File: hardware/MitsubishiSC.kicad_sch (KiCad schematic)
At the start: 68 parts, among them J1 CN105, J2 USB_C_Receptacle_USB2.0_16P, Q1 BSS138, Q2 BSS138, SW3 SPST, SW4 SPST, U1 TPS562203, U3 ESP32-C3-WROOM-02, U4 USBLC6-2SC6, U5 TLV75733PDBV

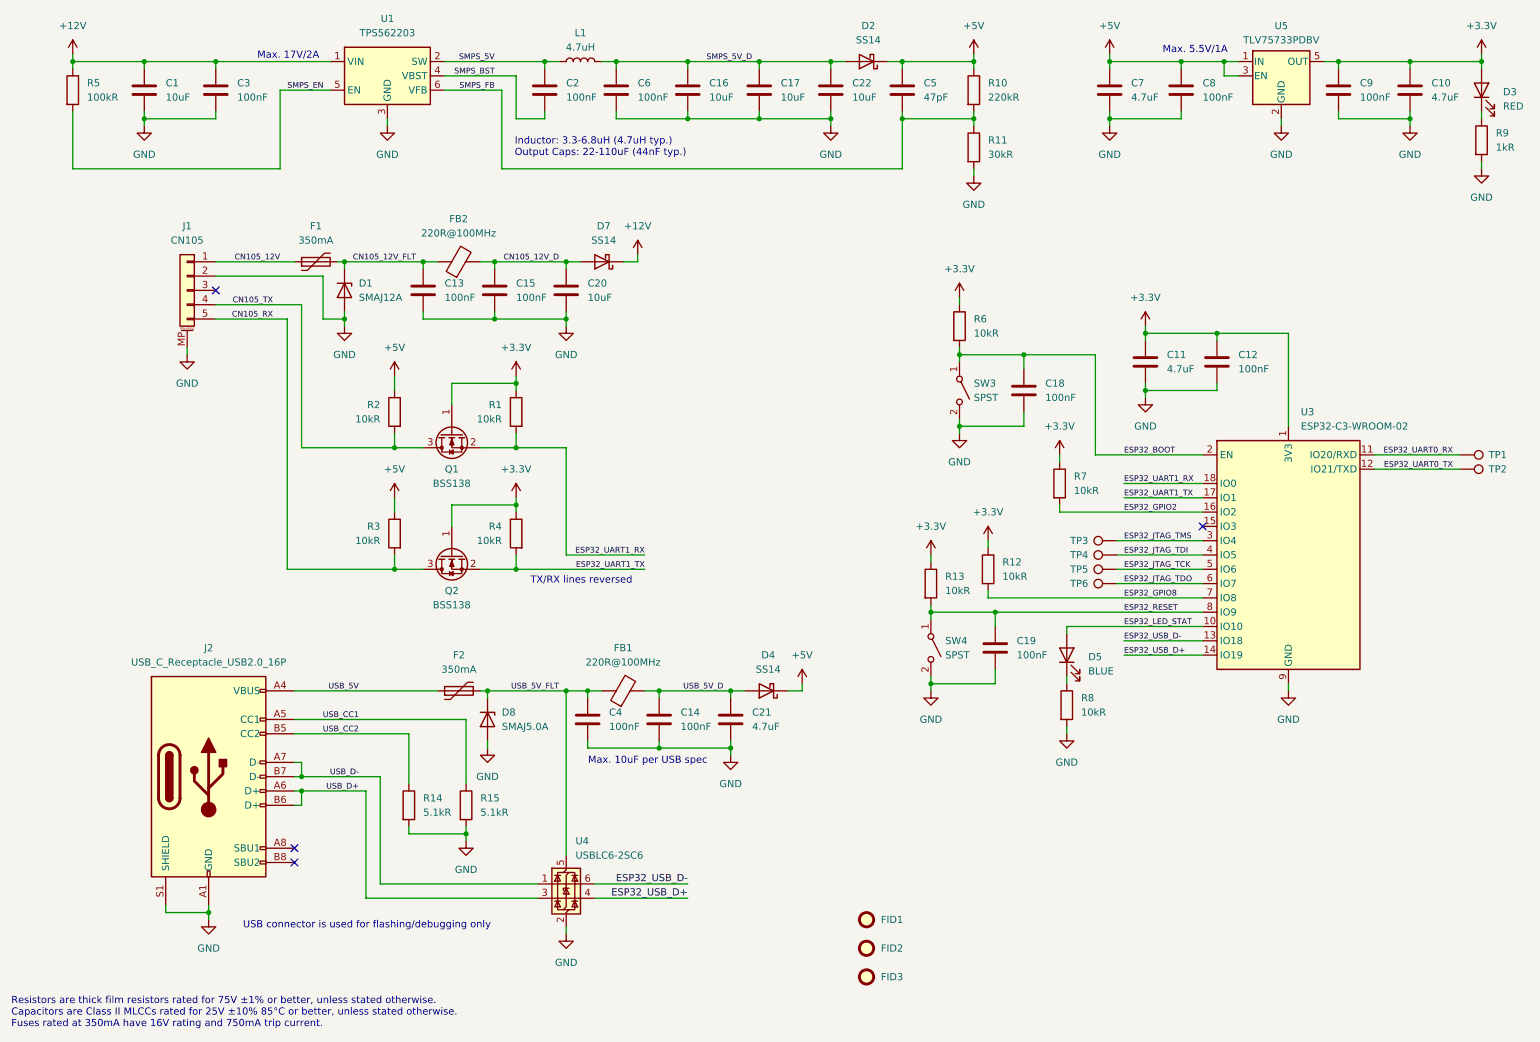
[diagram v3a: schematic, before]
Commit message: feat(pcb): revamp design and layout
This commit makes significant changes to the PCB, primarily changing the
MCU from ESP32-C3 to ESP32-C6 to accommodate Matter-over-Thread.
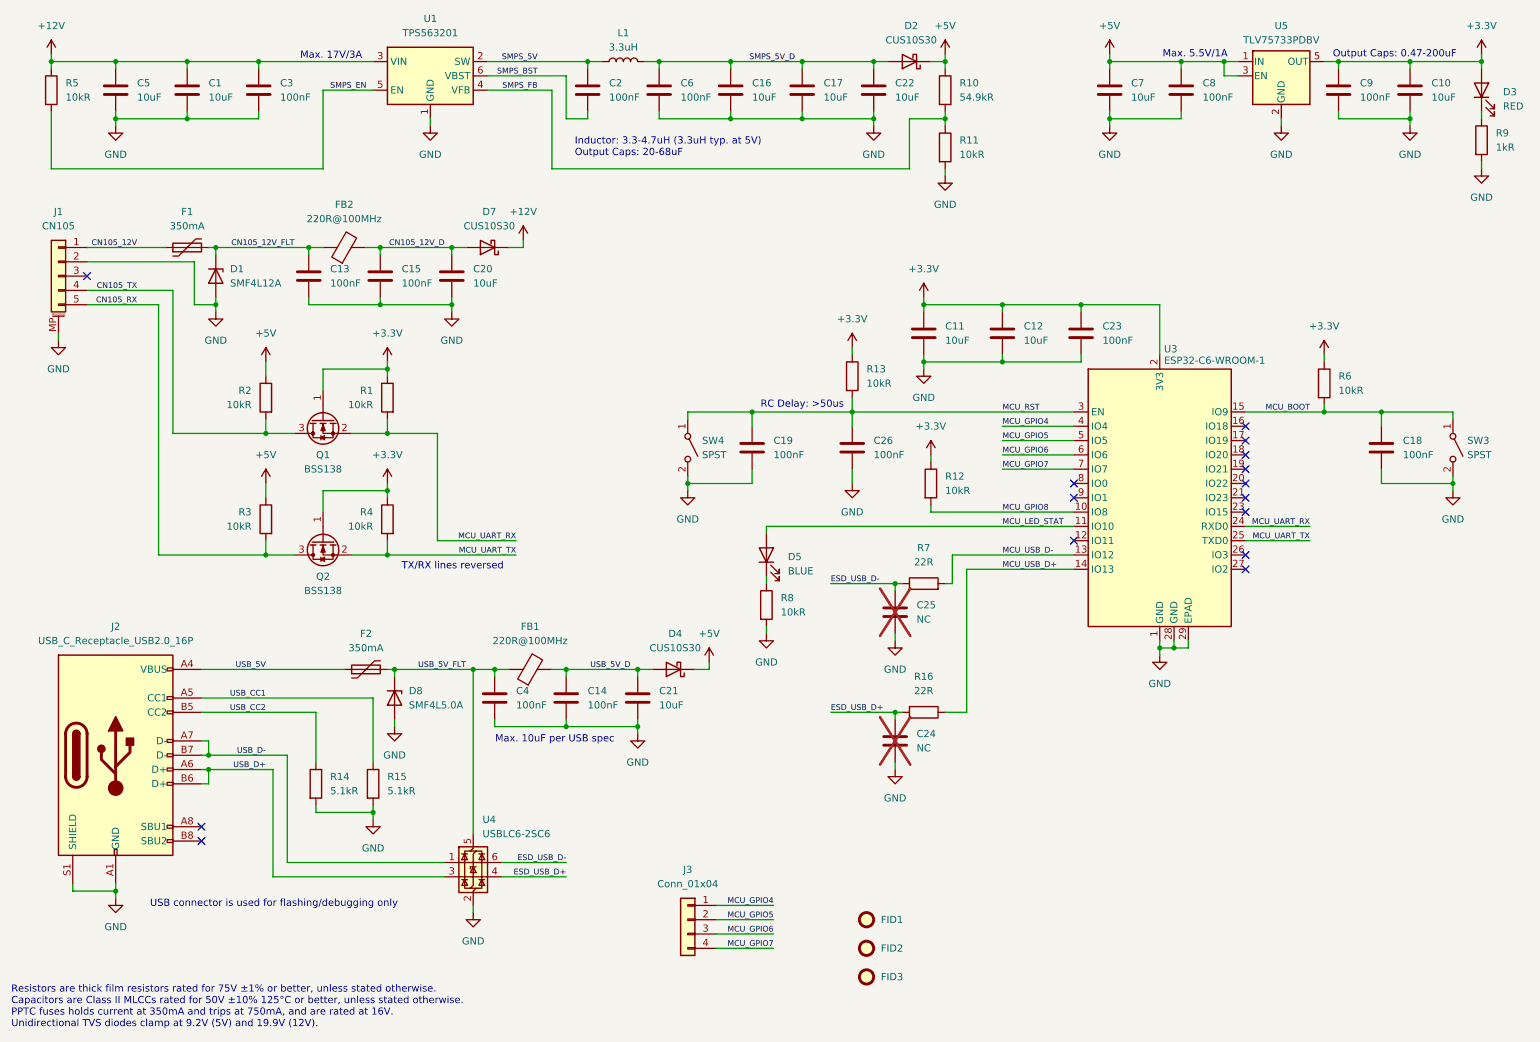
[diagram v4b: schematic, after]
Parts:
- removed TP1, TP2, TP3, TP4, TP5, TP6: TestPoint, TestPoint:TestPoint_Pad_D1.0mm, symbol Connector:TestPoint
- added C23, C26: 100nF, Capacitor_SMD:C_0603_1608Metric, symbol Device:C
- added C24, C25: NC, Capacitor_SMD:C_0603_1608Metric, symbol Device:C
- added J3: Conn_01x04, Connector_PinHeader_2.54mm:PinHeader_1x04_P2.54mm_Vertical, symbol Connector_Generic:Conn_01x04
- added R16: 22R, Resistor_SMD:R_0603_1608Metric, symbol Device:R
- C1, C16, C17, C20, C22: footprint Capacitor_SMD:C_0603_1608Metric -> Capacitor_SMD:C_1206_3216Metric; Distributor Part Number C344022 -> C89632; Manufacturer Murata Electronics -> Samsung Electro-Mechanics; Manufacturer Part Number GRM188R61E106KA73D -> CL31B106KBHNNNE
- C10, C11, C21, C7: value 4.7uF -> 10uF; footprint Capacitor_SMD:C_0603_1608Metric -> Capacitor_SMD:C_1206_3216Metric; Distributor Part Number C90057 -> C89632; Manufacturer Murata Electronics -> Samsung Electro-Mechanics; Manufacturer Part Number GRM188R61E475KE11D -> CL31B106KBHNNNE
- C12: value 100nF -> 10uF; footprint Capacitor_SMD:C_0603_1608Metric -> Capacitor_SMD:C_1206_3216Metric; Distributor Part Number C91183 -> C89632; Manufacturer YAGEO -> Samsung Electro-Mechanics; Manufacturer Part Number CC0603JRX7R9BB104 -> CL31B106KBHNNNE
- C13, C14, C15, C18, C19, C2, C3, C4, C6, C8, C9: Distributor Part Number C91183 -> C15725; Manufacturer YAGEO -> Samsung Electro-Mechanics; Manufacturer Part Number CC0603JRX7R9BB104 -> CL10B104KC8NNNC
- C5: value 47pF -> 10uF; footprint Capacitor_SMD:C_0603_1608Metric -> Capacitor_SMD:C_1206_3216Metric; Distributor Part Number C1671 -> C89632; Manufacturer Part Number CL10C470JB8NNNC -> CL31B106KBHNNNE
- D1: value SMAJ12A -> SMF4L12A; footprint Diode_SMD:D_SMA -> Diode_SMD:D_SOD-123F; Distributor Part Number C148213 -> C1972952; Manufacturer Part Number SMAJ12A -> SMF4L12A
- D2, D4, D7: value SS14 -> CUS10S30; footprint Diode_SMD:D_SMA -> Diode_SMD:D_SOD-323; Distributor Part Number C83852 -> C146335; Manufacturer onsemi -> TOSHIBA; Manufacturer Part Number SS14 -> CUS10S30,H3F
- D8: value SMAJ5.0A -> SMF4L5.0A; footprint Diode_SMD:D_SMA -> Diode_SMD:D_SOD-123F; Distributor Part Number C83329 -> C1976930; Manufacturer Part Number SMAJ5.0A -> SMF4L5.0A
- L1: value 4.7uH -> 3.3uH
- R10: value 220kR -> 54.9kR; Distributor Part Number C107696 -> C185321; Manufacturer Part Number RC0603FR-07220RL -> RC0603FR-0754K9L
- R11: value 30kR -> 10kR; Distributor Part Number C128060 -> C98220; Manufacturer Part Number RC0603FR-0730RL -> RC0603FR-0710KL
- R5: value 100kR -> 10kR; Distributor Part Number C14675 -> C98220; Manufacturer Part Number RC0603FR-07100KL -> RC0603FR-0710KL
- R7: value 10kR -> 22R; Distributor Part Number C98220 -> C107701; Manufacturer Part Number RC0603FR-0710KL -> RC0603FR-0722RL
- U1: value TPS562203 -> TPS563201; footprint Package_TO_SOT_SMD:SOT-563 -> Package_TO_SOT_SMD:SOT-23-6; symbol Regulator_Switching:TPS562203 -> _Custom:TPS563201; Distributor Part Number C22445511 -> C116592; Manufacturer Part Number TPS562203DRLR -> TPS563201DDCR
- U3: value ESP32-C3-WROOM-02 -> ESP32-C6-WROOM-1; footprint RF_Module:ESP32-C3-WROOM-02 -> _Custom:ESP32-C6-WROOM-1; symbol RF_Module:ESP32-C3-WROOM-02 -> _Custom:ESP32-C6-WROOM-1; Distributor Part Number C2934560 -> C5366877; Manufacturer Espressif Systems -> Espressif; Manufacturer Part Number ESP32-C3-WROOM-02-N4 -> ESP32-C6-WROOM-1-N8
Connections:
- net +12V: now also C5.1, U1.3 (VIN); no longer U1.1 (VIN)
- net +3.3V: now also U3.2 (3V3), C23.1; no longer R7.1, U3.1 (3V3)
- net +5V: no longer C5.1
- net GND: now also C5.2, U1.1 (GND), U3.1 (GND), U3.28 (GND), U3.29 (EPAD), C23.2, C24.2, C25.2, C26.2; no longer U1.3 (GND), U3.19 (GND), U3.9 (GND)
- net SMPS_BST: now also U1.6 (VBST); no longer U1.4 (VBST)
- net SMPS_FB: now also U1.4 (VFB); no longer C5.2, U1.6 (VFB)
- net MCU_BOOT: now reaches U3.15 (IO9)
- net MCU_BOOT: now also C18.1, R6.2, SW3.1 (A)
- removed net ESP32_BOOT: C18.1, R6.2, SW3.1 (A), U3.2 (EN)
- net ESP32_GPIO2: no longer names the net of U3.16 (IO18)
- net ESP32_GPIO2: no longer R7.2
- net ESP32_GPIO8 renamed MCU_GPIO7
- net MCU_GPIO7: now also J3.4 (Pin_4); no longer R12.2
- net ESP32_JTAG_TCK renamed MCU_GPIO5
- net MCU_GPIO5: now also J3.2 (Pin_2)
- net ESP32_JTAG_TDI renamed MCU_GPIO4
- net MCU_GPIO4: now also J3.1 (Pin_1)
- net ESP32_JTAG_TDO renamed MCU_GPIO6
- net MCU_GPIO6: now also J3.3 (Pin_3)
- net ESP32_JTAG_TMS renamed MCU_RST
- net MCU_RST: now also C19.1, R13.2, SW4.1 (A), C26.1
- net ESP32_LED_STAT renamed MCU_GPIO8
- net MCU_GPIO8: now also R12.2; no longer D5.2 (A)
- removed net ESP32_RESET: C19.1, R13.2, SW4.1 (A), U3.8 (IO9)
- net ESP32_UART0_RX renamed MCU_LED_STAT
- net MCU_LED_STAT: now also D5.2 (A)
- net ESP32_UART0_TX: no longer names the net of U3.12 (IO11)
- net ESP32_UART1_RX renamed MCU_UART_RX
- net MCU_UART_RX: now also U3.24 (RXD0); no longer U3.18 (IO0)
- net ESP32_UART1_TX renamed MCU_UART_TX
- net MCU_UART_TX: now also U3.25 (TXD0); no longer U3.17 (IO1)
- net ESP32_USB_D+ renamed ESD_USB_D+
- net ESD_USB_D+: now also C24.1, R16.2; no longer U3.14 (IO19)
- net ESP32_USB_D- renamed ESD_USB_D-
- net ESD_USB_D-: now also R7.1, C25.1; no longer U3.13 (IO18)
- new net MCU_USB_D+: R16.1, U3.14 (IO13)
- new net MCU_USB_D-: R7.2, U3.13 (IO12)
- no-connect marks 4 -> 15
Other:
- note added: "Inductor: 3.3-4.7uH (3.3uH typ. at 5V) Output Caps: 20-68uF"
- note added: "Max. 17V/3A"
- note added: "Output Caps: 0.47-200uF"
- note added: "RC Delay: >50us"
- note added: "Resistors are thick film resistors rated for 75V ±1% or better, unless stated otherwise. Capacitors are Class II MLCCs rated for 50V ±10% 125°C or better, unless stated otherwise. PPTC fuses holds current at 350mA and trips at 750mA, and are rated at 16V. Unidirectional TVS diodes clamp at 9.2V (5V) and 19.9V (12V)."
- note removed: "Inductor: 3.3-6.8uH (4.7uH typ.) Output Caps: 22-110uF (44nF typ.)"
- note removed: "Max. 17V/2A"
- note removed: "Resistors are thick film resistors rated for 75V ±1% or better, unless stated otherwise. Capacitors are Class II MLCCs rated for 25V ±10% 85°C or better, unless stated otherwise. Fuses rated at 350mA have 16V rating and 750mA trip current."
- moved on the sheet: C1, C11, C12, C13, C14, C15, C16, C17, C18, C19, C2, C20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

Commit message: feat: redesign PCB layout (#41)
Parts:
- removed C14, C2, C4, C6: 100nF, Capacitor_SMD:C_0603_1608Metric, symbol Device:C
- removed C21, C5: 10uF, Capacitor_SMD:C_1206_3216Metric, symbol Device:C
- removed C24, C25: NC, Capacitor_SMD:C_0603_1608Metric, symbol Device:C
- removed D4: CUS10S30, Diode_SMD:D_SOD-323, symbol Device:D_Schottky
- removed D5: BLUE, LED_SMD:LED_0805_2012Metric, symbol Device:LED
- removed D8: SMF4L5.0A, Diode_SMD:D_SOD-123F, symbol Device:D_Zener
- removed FB1: 220R@100MHz, Inductor_SMD:L_0805_2012Metric, symbol Device:FerriteBead
- removed J2: USB_C_Receptacle_USB2.0_16P, Connector_USB:USB_C_Receptacle_XKB_U262-16XN-4BVC11, symbol Connector:USB_C_Receptacle_USB2.0_16P
- removed J3: Conn_01x04, Connector_PinHeader_2.54mm:PinHeader_1x04_P2.54mm_Vertical, symbol Connector_Generic:Conn_01x04
- removed R10: 54.9kR, Resistor_SMD:R_0603_1608Metric, symbol Device:R
- removed R15: 5.1kR, Resistor_SMD:R_0603_1608Metric, symbol Device:R
- removed R16: 22R, Resistor_SMD:R_0603_1608Metric, symbol Device:R
- removed U1: TPS563201, Package_TO_SOT_SMD:SOT-23-6, symbol _Custom:TPS563201
- removed U3: ESP32-C6-WROOM-1, _Custom:ESP32-C6-WROOM-1, symbol _Custom:ESP32-C6-WROOM-1
- added C11: 100nF, Capacitor_SMD:C_0603_1608Metric, symbol Device:C
- added C16: 68pF, Capacitor_SMD:C_0603_1608Metric, symbol Device:C
- added C4: 100nF, Capacitor_SMD:C_0603_1608Metric, symbol Device:C_Small
- added D4: SMF4L5.0A, Diode_SMD:D_SOD-123F, symbol Device:D_Zener
- added D6: BU, LED_SMD:LED_0805_2012Metric, symbol Device:LED
- added H1, H2: #2, MountingHole:MountingHole_2.5mm_Pad_Via, symbol Mechanical:MountingHole_Pad
- added J2: TC2050, Connector:Tag-Connect_TC2050-IDC-NL_2x05_P1.27mm_Vertical, symbol Connector:TC2050
- added R12, R3, R4, R6: 0R, Resistor_SMD:R_0603_1608Metric, symbol Device:R
- added R13: 100kR, Resistor_SMD:R_0603_1608Metric, symbol Device:R
- added R19, R8: 10kR, Resistor_SMD:R_0603_1608Metric, symbol Device:R
- added U1: ESP32-C6-WROOM-1, _Custom:ESP32-C6-WROOM-1, symbol _Custom:ESP32-C6-WROOM-1
- added U2: TPS54202DDC, Package_TO_SOT_SMD:SOT-23-6, symbol Regulator_Switching:TPS54202DDC
- D5: renamed from D3; value RED -> RD
- F1: Manufacturer Part Number 1206L035/16 -> 1206L035/16YR
- F2: value 350mA -> 125mA; Distributor Part Number C126817 -> C151160; Manufacturer Part Number 1206L035/16 -> 1206L012WR
- L1: value 3.3uH -> 15uH; footprint Inductor_SMD:L_0603_1608Metric -> Inductor_SMD:L_TDK_VLS6045EX_VLS6045AF; Distributor Part Number C87515 -> C404502; Manufacturer Part Number MLF1608A4R7JT000 -> VLS6045EX-150M
- R11: value 10kR -> 0R; Distributor Part Number C98220 -> C100044; Manufacturer Part Number RC0603FR-0710KL -> RC0603FR-070RL
- R14: value 5.1kR -> 13.3kR; Distributor Part Number C105580 -> C185373; Manufacturer Part Number RC0603FR-075K1L -> RC0603FR-0713K3L
- R5: value 10kR -> 470R; Distributor Part Number C98220 -> C114669; Manufacturer Part Number RC0603FR-0710KL -> RC0603FR-07470RL
- R7: value 22R -> 0R; Distributor Part Number C107701 -> C100044; Manufacturer Part Number RC0603FR-0722RL -> RC0603FR-070RL
- R9: value 1kR -> 0R; Distributor Part Number C22548 -> C100044; Manufacturer Part Number RC0603FR-071KL -> RC0603FR-070RL
- SW1: renamed from SW4; footprint Button_Switch_SMD:SW_SPST_B3U-1000P -> Button_Switch_SMD:SW_SPST_PTS810; Distributor Part Number C231329 -> C843674; Manufacturer Omron Electronics -> G-Switch; Manufacturer Part Number B3U-1000P -> GT-TC048D-H025-L1
- SW2: renamed from SW3; footprint Button_Switch_SMD:SW_SPST_B3U-1000P -> Button_Switch_SMD:SW_SPST_PTS810; Distributor Part Number C231329 -> C843674; Manufacturer Omron Electronics -> G-Switch; Manufacturer Part Number B3U-1000P -> GT-TC048D-H025-L1
- renumbered C11 to C1, C16 to C13, C17 to C14, C22 to C15, C13 to C17, C15 to C18, C20 to C19, C23 to C2, C19 to C20, C18 to C21, C26 to C3, C1 to C5, C3 to C6, D2 to D1, D7 to D2, D1 to D3, FB2 to FB1, R13 to R1, R12 to R10, R2 to R15, R1 to R16, R3 to R17, R4 to R18, R6 to R2, R8 to R20, U5 to U3
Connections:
- net CN105_12V_D is gone; now on net CN105_12V_FLT: C18.1, C19.1, D2.2 (A), FB1.2
- net USB_5V is gone; now on net CN105_5V: F2.1
- net USB_CC2 is gone; now on net SMPS_FB: R14.1
- net USB_D+ is gone; now on net CN105_RX: U4.3 (I/O2)
- net USB_D- is gone; now on net CN105_TX: U4.1 (I/O1)
- net +12V: now also U2.3 (VIN); no longer R5.1
- net +3.3V: now also J2.1, U1.2 (3V3); no longer C12.1
- net +5V: now also C16.1, R13.1; no longer R15.1, R17.1
- net CN105_12V_FLT: no longer C17.1, D3.1 (K), F1.2, FB1.1
- net CN105_RX: no longer Q2.3 (D), R17.2
- net CN105_TX: no longer Q1.3 (D), R15.2
- net GND: now also C11.2, D4.2 (A), H1.1, H2.1, J2.2, J2.3, R19.2, R8.2, U1.1 (GND), U1.28 (GND), U1.29 (EPAD), U2.1 (GND); no longer R11.2, R9.2
- net MCU_BOOT: now also U1.15 (IO9)
- net MCU_RST: now also U1.3 (EN)
- net SMPS_FB: now also C16.2, R13.2, U2.4 (FB); no longer R11.1
- net MCU_LED_K: now reaches R20.1
- net MCU_LED_K: now also D6.1 (K)
- net CN105_5V: now reaches J1.3 (5V)
- net DBG_JTDO: now reaches R9.1
- net DBG_JTDO: now also J2.8; no longer D5.1 (K)
- net ESD_USB_D+ renamed CN105_RXH
- net CN105_RXH: now also Q2.3 (D), R17.2
- net ESD_USB_D- renamed CN105_TXH
- net CN105_TXH: now also Q1.3 (D), R15.2; no longer R7.1
- net MCU_GPIO8 renamed MCU_IO08
- net MCU_IO08: now also U1.10 (IO8)
- net MCU_UART_RX renamed CN105_TXL
- net CN105_TXL: now also R6.2
- net MCU_UART_TX renamed CN105_RXL
- net CN105_RXL: now also R5.1
- net MCU_USB_D- renamed DBG_JTCK
- net DBG_JTCK: now also J2.9
- net SMPS_5V renamed SMPS_SW
- net SMPS_SW: now also C4.2, U2.2 (SW)
- net SMPS_5V_D renamed SMPS_SW_5V
- net SMPS_SW_5V: now also C12.1, C11.1
- net SMPS_EN renamed MCU_TX1
- net MCU_TX1: now also U1.20 (IO22)
- net USB_5V_FLT renamed CN105_5V_FSD
- net CN105_5V_FSD: now also R15.1, R17.1, D4.1 (K)
- new net CN105_12V_FSD: C17.1, D3.1 (K), F1.2, FB1.1
- new net DBG_JTDI: J2.7, R4.2
- new net DBG_JTMS: J2.10, R3.1
- new net DBG_RXD: J2.5, R12.2
- new net DBG_TXD: J2.4, R11.1
- new net MCU_3V3_K: D5.1 (K), R19.1
- new net MCU_IO15: R8.1, U1.23 (IO15)
- new net MCU_LED: D6.2 (A), U1.17 (IO19)
- new net MCU_MTCK: R7.1, U1.6 (IO6)
- new net MCU_MTDI: R4.1, U1.5 (IO5)
- new net MCU_MTDO: R9.2, U1.7 (IO7)
- new net MCU_MTMS: R3.2, U1.4 (IO4)
- new net MCU_RX0: R11.2, U1.24 (RXD0)
- new net MCU_RX1: R6.1, U1.21 (IO23)
- new net MCU_TX0: R12.1, U1.25 (TXD0)
- new net SMPS_BOOT: C4.1, U2.6 (BOOT)
- no-connect marks 15 -> 13
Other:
- note added: "0.47-200uF"
- note added: "15-33uH"
- note added: "44-68uF"
- note added: "EN: Floating = Enabled"
- note added: "Max. 28V/2A"
- note added: "Ref. 0.596V"
- note added: "Resistors are thick film resistors rated for 75V ±1% or better, unless stated otherwise. Capacitors are Class II MLCCs rated for 50V ±10% 125°C or better, unless stated otherwise. PPTC fuses trip at 750mA (350mA) and 290mA (125mA), and are rated at 16V or better. Unidirectional TVS diodes clamp at 9.2V (5V) and 19.9V (12V)."
- note added: "TX/RX inverted"
- note removed: "Inductor: 3.3-4.7uH (3.3uH typ. at 5V) Output Caps: 20-68uF"
- note removed: "Max. 10uF per USB spec"
- note removed: "Max. 17V/3A"
- note removed: "Output Caps: 0.47-200uF"
- note removed: "Resistors are thick film resistors rated for 75V ±1% or better, unless stated otherwise. Capacitors are Class II MLCCs rated for 50V ±10% 125°C or better, unless stated otherwise. PPTC fuses holds current at 350mA and trips at 750mA, and are rated at 16V. Unidirectional TVS diodes clamp at 9.2V (5V) and 19.9V (12V)."
- note removed: "TX/RX lines reversed"
- note removed: "USB connector is used for flashing/debugging only"
- moved on the sheet: C1, C10, C13, C14, C15, C17, C18, C19, C2, C20, C21, C3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
